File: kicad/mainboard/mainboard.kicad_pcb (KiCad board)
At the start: 2 copper layers, 41.9 x 78.7 mm, 8 parts, among them J1 Conn_01x11_Female, J2 Screw_Terminal_01x02, J3 Conn_01x06_Female, J4 Screw_Terminal_01x02, U1 34.81-8240

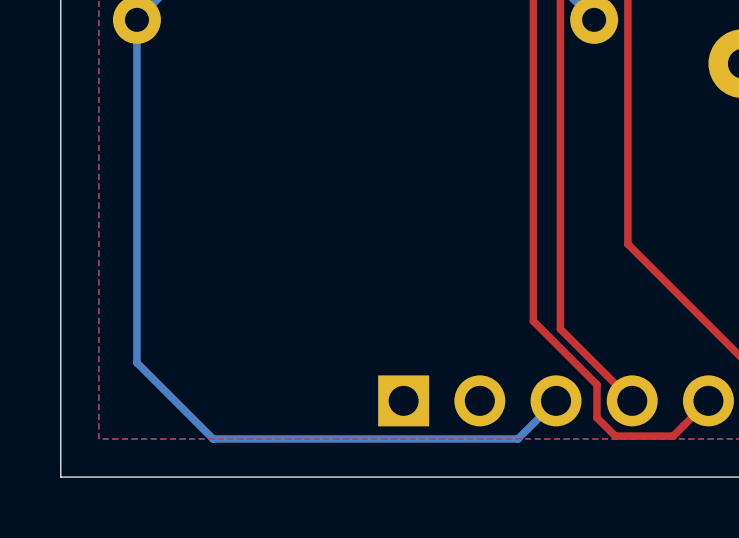
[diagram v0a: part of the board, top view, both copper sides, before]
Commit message: Fix up a couple of errors on the mainboard PCB
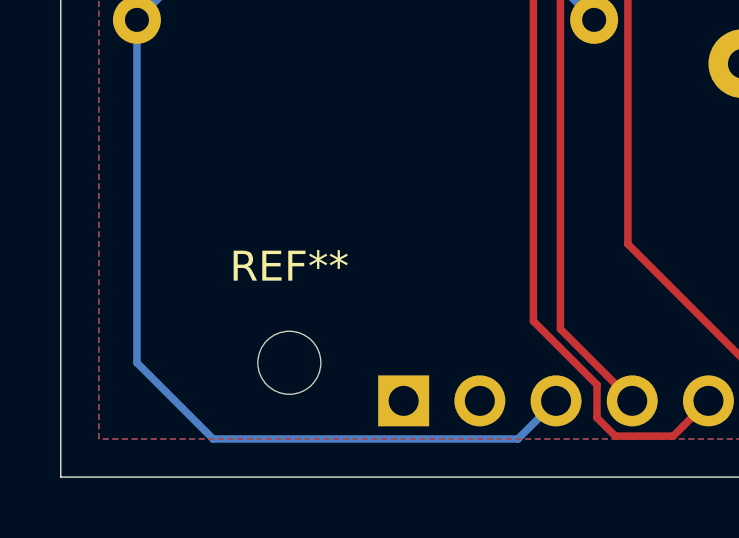
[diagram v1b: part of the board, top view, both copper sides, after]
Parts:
- added REF**: MountingHole_2.1mm, MountingHole:MountingHole_2.1mm, F.Cu at (118.1, 102.9)
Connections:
- U1 pad A1: Net-(A1-Pad13) -> Net-(A1-Pad29)
- U1 pad A2: Net-(A1-Pad29) -> Net-(A1-Pad13)
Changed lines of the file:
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@@
     (tracks 96)
     (zones 0)
-    (modules 8)
+    (modules 9)
     (nets 35)
   )
@@
     (mod_text_size 1 1)
     (mod_text_width 0.15)
-    (pad_size 1.9 1.9)
-    (pad_drill 1.15)
+    (pad_size 1.778 1.778)
+    (pad_drill 0.95)
     (pad_to_mask_clearance 0.051)
     (solder_mask_min_width 0.25)
@@
       (outputformat 1)
       (mirror false)
-      (drillshape 1)
+      (drillshape 0)
       (scaleselection 1)
       (outputdirectory ""))
@@
     (add_net "Net-(J4-Pad1)")
     (add_net "Net-(J4-Pad2)")
+  )
+  (module MountingHole:MountingHole_2.1mm (layer F.Cu)
+    (at 118.11 102.87)
+    (descr "Mounting Hole 2.1mm, no annular")
+    (tags "mounting hole 2.1mm no annular")
+    (attr virtual)
+    (fp_text reference REF** (at 0 -3.2) (layer F.SilkS)
+      (effects (font (size 1 1) (thickness 0.15)))
+    )
+    (fp_text value MountingHole_2.1mm (at 0 3.2) (layer F.Fab)
+      (effects (font (size 1 1) (thickness 0.15)))
+    )
+    (fp_circle (center 0 0) (end 2.35 0) (layer F.CrtYd) (width 0.05))
+    (fp_circle (center 0 0) (end 2.1 0) (layer Cmts.User) (width 0.15))
+    (fp_text user %R (at 0.3 0) (layer F.Fab)
+      (effects (font (size 1 1) (thickness 0.15)))
+    )
+    (pad "" np_thru_hole circle (at 0 0) (size 2.1 2.1) (drill 2.1) (layers *.Cu *.Mask))
   )
   (module Module:Arduino_Nano (layer B.Cu)
@@
     (fp_line (start -1.59 1.32) (end -0.1 1.32) (layer B.SilkS) (width 0.12))
     (fp_line (start -0.32 1.05) (end -1.32 0.04) (layer B.Fab) (width 0.1))
-    (pad A2 thru_hole circle (at 2.54 0 90) (size 1.778 1.778) (drill 0.95) (layers *.Cu *.Mask)
+    (pad A1 thru_hole circle (at 2.54 0 90) (size 1.778 1.778) (drill 0.95) (layers *.Cu *.Mask)
       (net 7 "Net-(A1-Pad29)"))
-    (pad A1 thru_hole rect (at 0 0 90) (size 1.778 1.778) (drill 0.95) (layers *.Cu *.Mask)
+    (pad A2 thru_hole rect (at 0 0 90) (size 1.778 1.778) (drill 0.95) (layers *.Cu *.Mask)
       (net 25 "Net-(A1-Pad13)"))
     (pad 11 thru_hole circle (at 12.7 0 90) (size 1.9 1.9) (drill 1.15) (layers *.Cu *.Mask)
